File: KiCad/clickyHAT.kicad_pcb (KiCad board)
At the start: 2 copper layers, 65 x 56.5 mm, 22 parts, among them J1 Raspberry_Pi_2_3, Q1 BS170, SW1 SW_Push, SW2 SW_Push, SW3 SW_Push, SW4 SW_Push

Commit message: removed board logo until license is decided
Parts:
- removed REF***: OSHW-Symbol_6.7x6mm_SilkScreen, Symbols:OSHW-Symbol_6.7x6mm_SilkScreen
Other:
- board text added: "Raspberry Pi add-on board for mechanical keyboard switches"
- board text added: "clickyBoard"
- board text removed: "A HAT for mechanical keyboard switches"
- board text removed: "ClickyHAT"

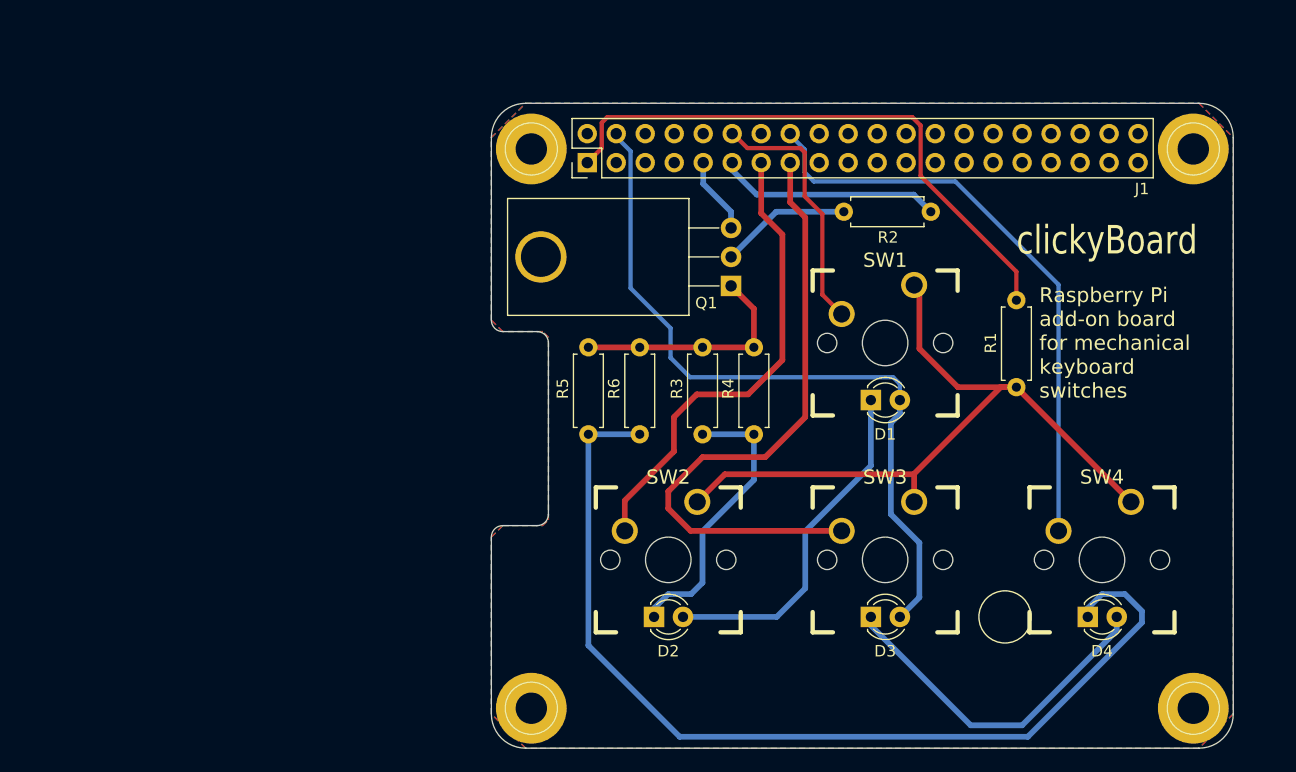
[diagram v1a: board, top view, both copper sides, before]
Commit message: Updated board design
removed copper fill, updated gerbers are included
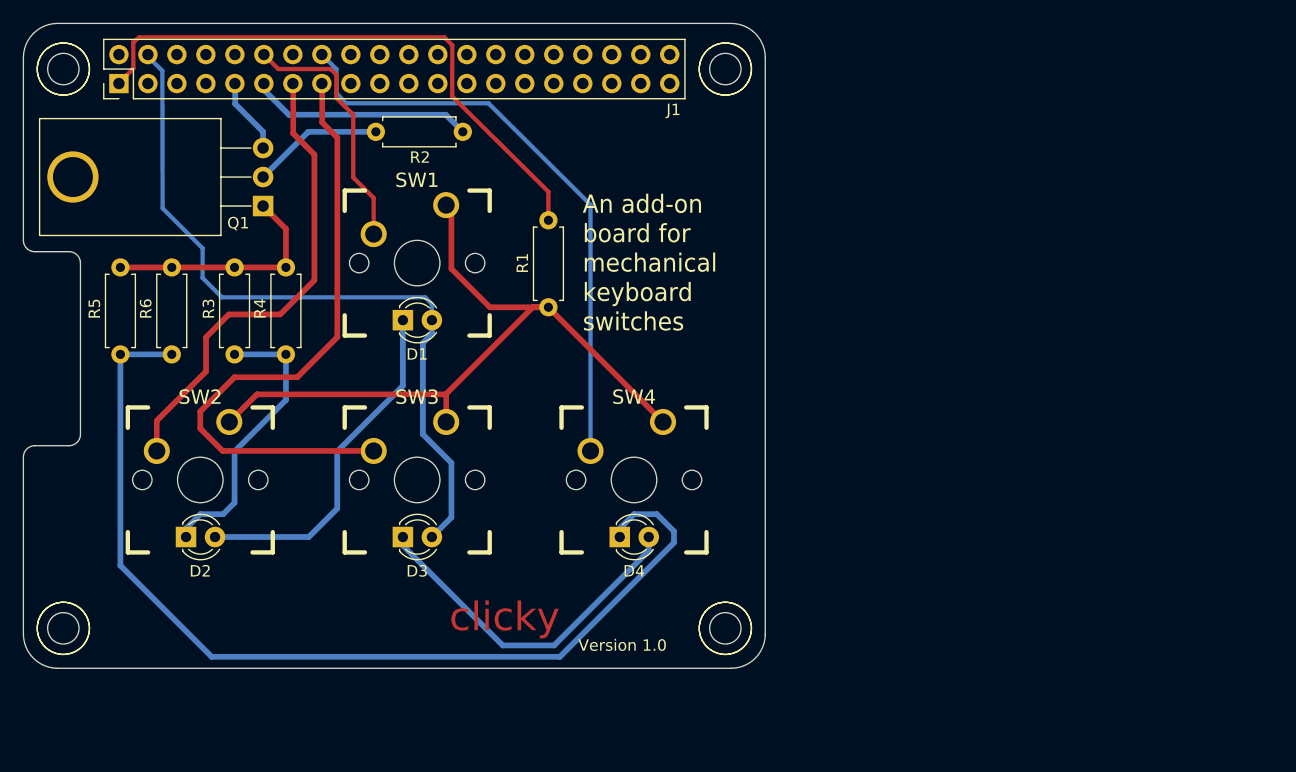
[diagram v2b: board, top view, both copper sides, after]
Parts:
- removed CAM: 1pin, Connectors:1pin
- added MNT1: 1pin, Connectors:1pin, F.Cu at (47.5, 77.0)
- added MNT3: 1pin, Connectors:1pin, F.Cu at (47.5, 126.0)
- added MNT4: 1pin, Connectors:1pin, F.Cu at (105.5, 126.0)
- added MNTB2: 1pin, Connectors:1pin, F.Cu at (105.5, 77.0)
- added REF***: OSHW-Logo_11.4x12mm_SilkScreen, Symbols:OSHW-Logo_11.4x12mm_SilkScreen, B.Cu at (100.0, 95.0)
- moved J1 41.6 mm to (52.4, 78.3)
- moved D1 41.6 mm to (77.2, 99.0)
- moved D2 41.6 mm to (58.2, 118.0)
- moved D3 41.6 mm to (77.2, 118.0)
- moved D4 41.6 mm to (96.2, 118.0)
- moved MNT2 41.6 mm to (105.5, 77.0)
- moved MNTB1 41.6 mm to (47.5, 77.0)
- moved MNTB3 41.6 mm to (47.5, 126.0)
- moved MNTB4 41.6 mm to (105.5, 126.0)
- moved Q1 41.6 mm to (65.0, 89.0)
- moved R1 41.6 mm to (90.0, 90.2)
- moved R2 41.6 mm to (82.5, 82.5)
- moved R3 41.6 mm to (62.5, 102.0)
- moved R4 41.6 mm to (67.0, 102.0)
- moved R5 41.6 mm to (52.5, 102.0)
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- renumbered MNT1 to MNTB1, MNT3 to MNTB3, MNT4 to MNTB4
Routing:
- removed copper zone on B.Cu, net (none)
- removed copper zone on F.Cu, net (none)
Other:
- net class Default: trace_width 0.25 -> 0.375
- board text added: "An add-on board for mechanical keyboard switches"
- board text added: "Board"
- board text added: "CC BY-SA 4.0"
- board text added: "Version 1.0"
- board text added: "clicky"
- board text added: "design by Jack Kelly"
- board text removed: "Raspberry Pi add-on board for mechanical keyboard switches"
- board text removed: "clickyBoard"

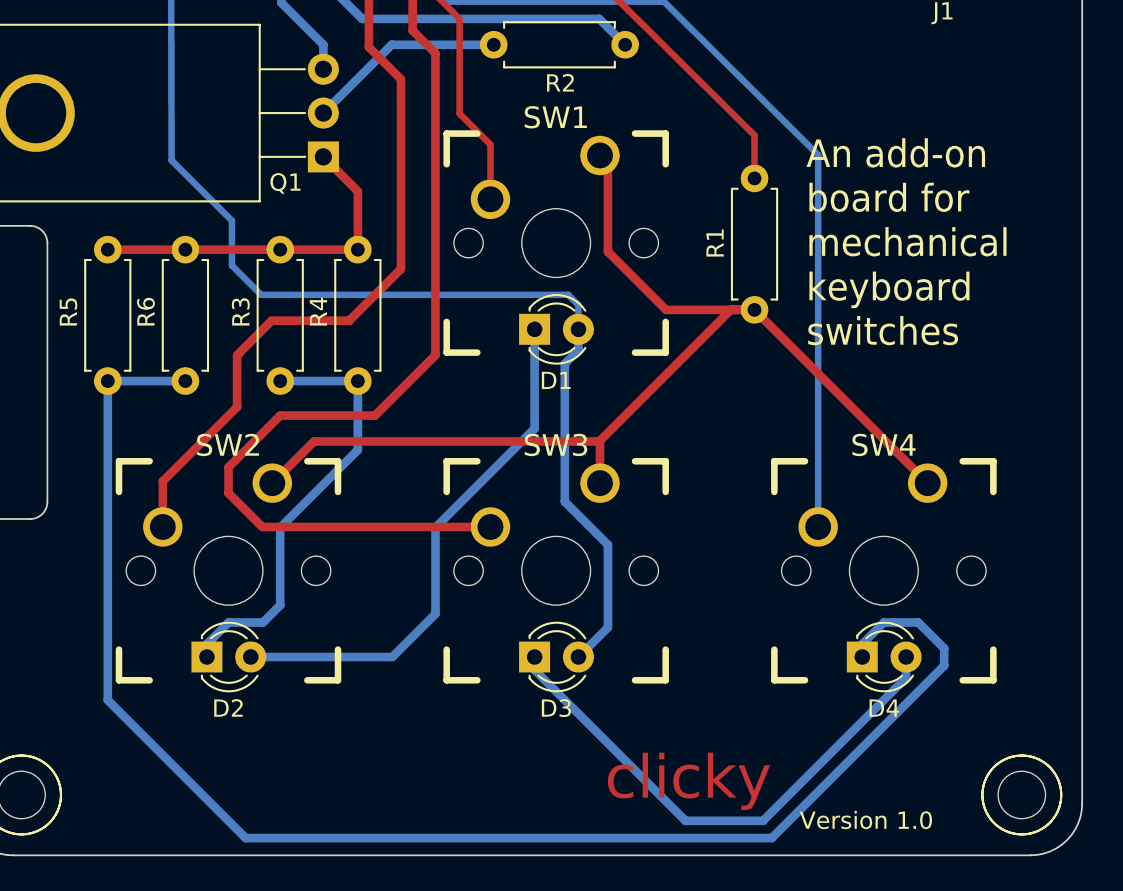
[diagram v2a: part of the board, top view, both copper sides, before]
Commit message: updated board text
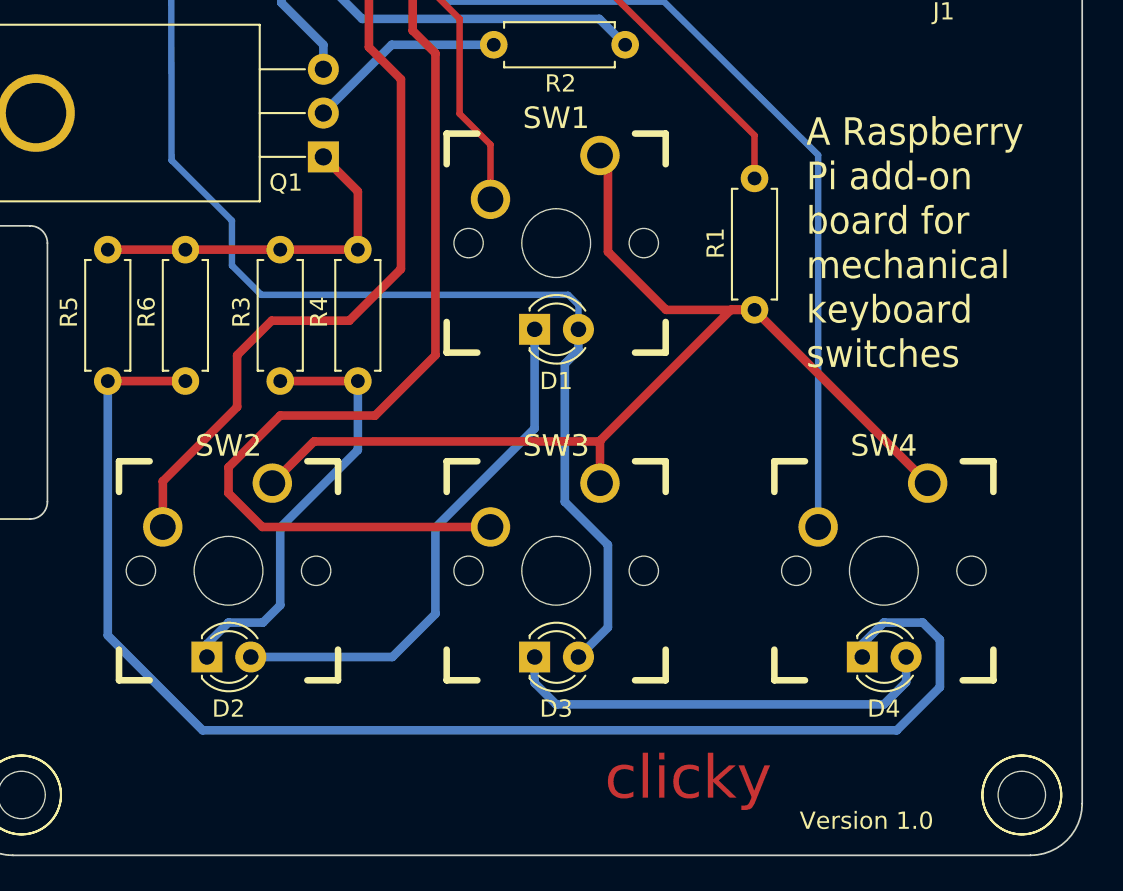
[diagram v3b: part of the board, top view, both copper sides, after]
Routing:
- net Net-(D4-Pad1): track 86.6 -> 79.7 mm
- net Net-(D3-Pad1): track 30.6 -> 26.3 mm
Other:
- board text added: "A Raspberry Pi add-on board for mechanical keyboard switches"
- board text removed: "An add-on board for mechanical keyboard switches"
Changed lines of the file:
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@@
     (thickness 1.6)
     (drawings 24)
-    (tracks 113)
+    (tracks 114)
     (zones 0)
     (modules 25)
@@
   )
   (layers
-    (0 F.Cu signal hide)
+    (0 F.Cu signal)
     (31 B.Cu signal)
     (32 B.Adhes user)
@@
     (arrow2b (pts (xy 47.5 70.5) (xy 48.626504 69.913579)))
   )
-  (gr_text "An add-on\nboard for\nmechanical\nkeyboard\nswitches" (at 93 94) (layer F.SilkS)
+  (gr_text "A Raspberry\nPi add-on\nboard for\nmechanical\nkeyboard\nswitches" (at 93 94) (layer F.SilkS)
     (effects (font (size 1.6 1.5) (thickness 0.15)) (justify left))
   )
@@
   (segment (start 79 101) (end 79 109) (width 0.5) (layer B.Cu) (net 2))
   (segment (start 79.79 100.21) (end 79 101) (width 0.5) (layer B.Cu) (net 2))
-  (segment (start 67 102) (end 62.5 102) (width 0.5) (layer B.Cu) (net 3))
+  (segment (start 67 102) (end 62.5 102) (width 0.5) (layer F.Cu) (net 3))
   (segment (start 58.25 118) (end 58.25 117.25) (width 0.5) (layer B.Cu) (net 3))
   (segment (start 58.25 117.25) (end 59.5 116) (width 0.5) (layer B.Cu) (net 3))
@@
   (segment (start 62.5 110.5) (end 67 106) (width 0.5) (layer B.Cu) (net 3))
   (segment (start 67 106) (end 67 102) (width 0.5) (layer B.Cu) (net 3))
+  (segment (start 77.25 118) (end 77.25 119.5) (width 0.5) (layer B.Cu) (net 4))
+  (segment (start 98.79 119.46) (end 98.79 118) (width 0.5) (layer B.Cu) (net 4))
+  (segment (start 97.5 120.75) (end 98.79 119.46) (width 0.5) (layer B.Cu) (net 4))
+  (segment (start 78.5 120.75) (end 97.5 120.75) (width 0.5) (layer B.Cu) (net 4))
+  (segment (start 77.25 119.5) (end 78.5 120.75) (width 0.5) (layer B.Cu) (net 4))
   (segment (start 77.25 118) (end 77.25 118.75) (width 0.5) (layer B.Cu) (net 4))
-  (segment (start 77.25 118.75) (end 86 127.5) (width 0.5) (layer B.Cu) (net 4))
-  (segment (start 86 127.5) (end 90.5 127.5) (width 0.5) (layer B.Cu) (net 4))
-  (segment (start 90.5 127.5) (end 98.79 119.21) (width 0.5) (layer B.Cu) (net 4))
-  (segment (start 98.79 119.21) (end 98.79 118) (width 0.5) (layer B.Cu) (net 4))
-  (segment (start 52.5 102) (end 57 102) (width 0.5) (layer B.Cu) (net 5))
+  (segment (start 57 102) (end 52.5 102) (width 0.5) (layer F.Cu) (net 5))
   (segment (start 96.25 118) (end 96.25 117.25) (width 0.5) (layer B.Cu) (net 5))
   (segment (start 96.25 117.25) (end 97.5 116) (width 0.5) (layer B.Cu) (net 5))
-  (segment (start 97.5 116) (end 99.5 116) (width 0.5) (layer B.Cu) (net 5))
-  (segment (start 99.5 116) (end 101 117.5) (width 0.5) (layer B.Cu) (net 5))
-  (segment (start 101 117.5) (end 101 118.5) (width 0.5) (layer B.Cu) (net 5))
-  (segment (start 101 118.5) (end 91 128.5) (width 0.5) (layer B.Cu) (net 5))
-  (segment (start 91 128.5) (end 60.5 128.5) (width 0.5) (layer B.Cu) (net 5))
-  (segment (start 60.5 128.5) (end 52.5 120.5) (width 0.5) (layer B.Cu) (net 5))
-  (segment (start 52.5 120.5) (end 52.5 102) (width 0.5) (layer B.Cu) (net 5))
+  (segment (start 97.5 116) (end 99.75 116) (width 0.5) (layer B.Cu) (net 5))
+  (segment (start 99.75 116) (end 100.75 117) (width 0.5) (layer B.Cu) (net 5))
+  (segment (start 100.75 117) (end 100.75 119.75) (width 0.5) (layer B.Cu) (net 5))
+  (segment (start 100.75 119.75) (end 98.25 122.25) (width 0.5) (layer B.Cu) (net 5))
+  (segment (start 98.25 122.25) (end 58 122.25) (width 0.5) (layer B.Cu) (net 5))
+  (segment (start 58 122.25) (end 52.5 116.75) (width 0.5) (layer B.Cu) (net 5))
+  (segment (start 52.5 116.75) (end 52.5 102) (width 0.5) (layer B.Cu) (net 5))
   (segment (start 90 90.25) (end 90 87.75) (width 0.375) (layer F.Cu) (net 6))
   (segment (start 53.637747 76.93845) (end 52.4 78.2) (width 0.375) (layer F.Cu) (net 6))

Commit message: Revision 1.1
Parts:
- R3, R4, R5, R6: value 100 -> 150
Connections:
- D2 pad 2: Net-(D1-Pad1) -> Net-(D1-Pad2)
- D4 pad 2: Net-(D3-Pad1) -> Net-(D1-Pad2)
- J1 pad 39: Net-(J1-Pad39) -> Net-(J1-Pad25)
- J1 pad 9: Net-(J1-Pad9) -> Net-(J1-Pad25)
- Q1 pad 1: Net-(Q1-Pad1) -> Net-(Q1-Pad2)
- Q1 pad 2: Net-(Q1-Pad2) -> Net-(Q1-Pad1)
- Q1 pad 3: Net-(J1-Pad9) -> Net-(J1-Pad25)
- R4 pad 1: Net-(D2-Pad1) -> Net-(D1-Pad1)
- R6 pad 1: Net-(D4-Pad1) -> Net-(D3-Pad1)
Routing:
- net Net-(D1-Pad2): track 65.1 -> 134.0 mm
- net Net-(J1-Pad15): track 55.0 -> 34.8 mm
- net Net-(D1-Pad1): track 30.6 -> 11.5 mm
- net Net-(D3-Pad1): track 26.3 -> 43.6 mm
- net Net-(D4-Pad1): track 79.7 -> 63.6 mm
- net Net-(J1-Pad9): track 6.73 -> 0.00 mm
- net Net-(J1-Pad25): track 0.00 -> 6.72 mm
- net Net-(J1-Pad12): track 22.4 -> 27.8 mm
- net Net-(J1-Pad16): track 52.7 -> 49.2 mm
- net Net-(Q1-Pad1): track 20.7 -> 23.8 mm
- net Net-(R1-Pad2): track 64.4 -> 61.7 mm
- net Net-(J1-Pad1): track 51.3 -> 48.7 mm
- net Net-(J1-Pad13): track 41.7 -> 40.6 mm
- net Net-(Q1-Pad2): track 11.5 -> 12.7 mm
- net Net-(D2-Pad1): track 25.3 -> 24.7 mm
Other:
- board text added: "Version 1.1"
- board text removed: "Version 1.0"

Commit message: Documentation updated
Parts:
- moved R3 10.0 mm to (52.5, 102.0)
- moved R4 10.0 mm to (57.0, 102.0)
- moved R5 10.0 mm to (62.5, 102.0)
- moved R6 10.0 mm to (67.0, 102.0)
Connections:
- J1 pad 39: Net-(J1-Pad25) -> Net-(J1-Pad39)
- J1 pad 9: Net-(J1-Pad25) -> Net-(J1-Pad9)
- Q1 pad 3: Net-(J1-Pad25) -> Net-(J1-Pad9)
- R3 pad 1: Net-(D2-Pad1) -> Net-(D4-Pad1)
- R4 pad 1: Net-(D1-Pad1) -> Net-(D3-Pad1)
- R5 pad 1: Net-(D4-Pad1) -> Net-(D2-Pad1)
- R6 pad 1: Net-(D3-Pad1) -> Net-(D1-Pad1)
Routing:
- net Net-(J1-Pad9): track 0.00 -> 6.72 mm
- net Net-(J1-Pad25): track 6.72 -> 0.00 mm
- added copper zone on F.Cu, net Net-(Q1-Pad1)
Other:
- board text added: "GPIO 12"
- board text added: "GPIO 13"
- board text added: "GPIO 15"
- board text added: "GPIO 16"
- board text added: "LEDs GPIO 11"

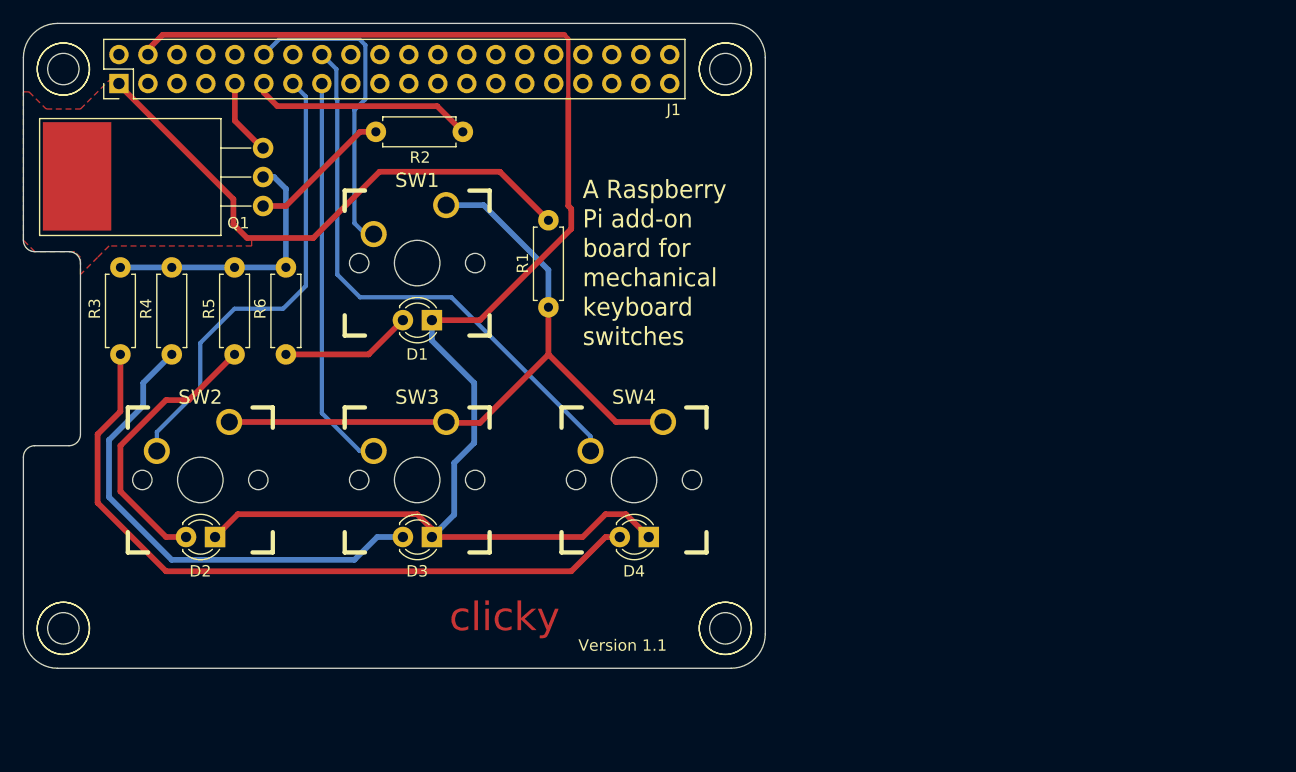
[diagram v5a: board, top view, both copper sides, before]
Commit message: Rotated switches
crazy routing
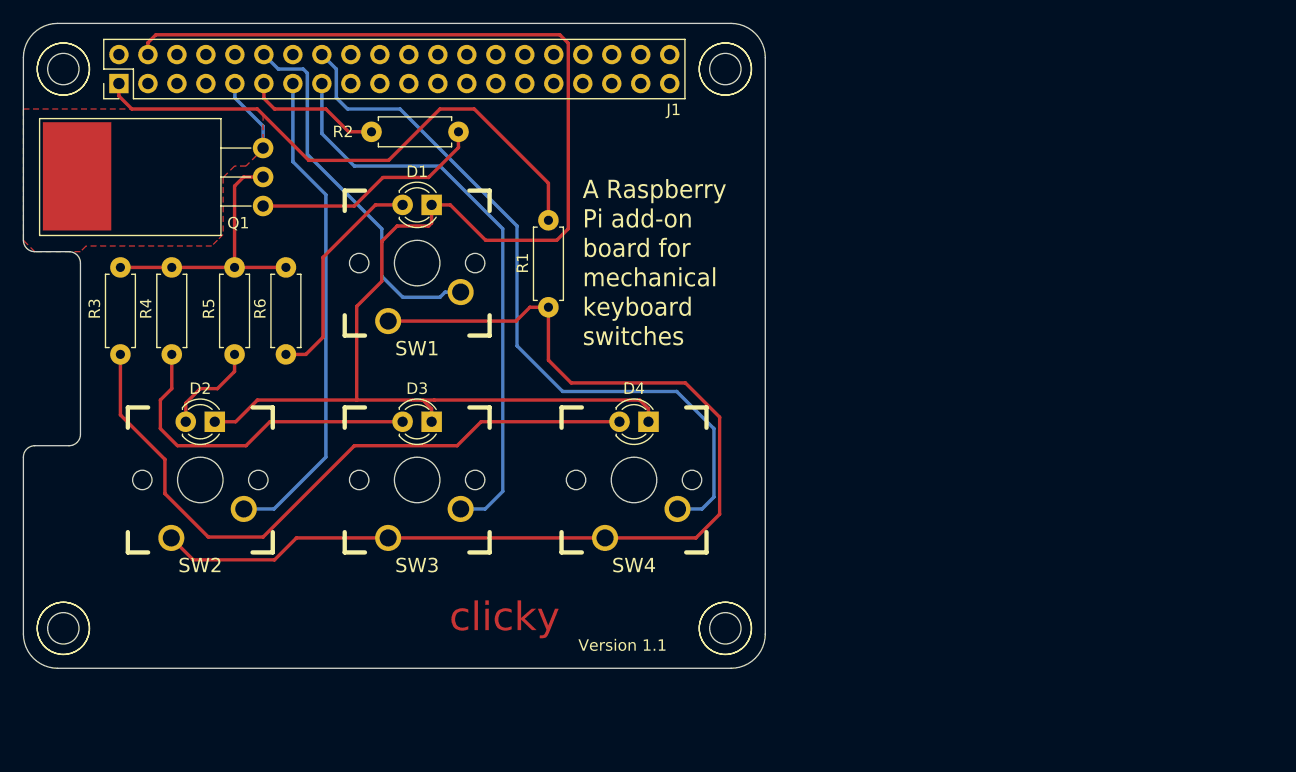
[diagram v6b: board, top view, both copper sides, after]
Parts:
- moved D1 10.1 mm to (77.2, 88.9)
- moved D2 10.1 mm to (58.2, 107.9)
- moved D3 10.1 mm to (77.2, 107.9)
- moved D4 10.1 mm to (96.2, 107.9)
- moved R2 8.00 mm to (74.5, 82.5), turned to 0 degrees
- turned SW1 to 180 degrees
- turned SW2 to 180 degrees
- turned SW3 to 180 degrees
- turned SW4 to 180 degrees
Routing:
- net Net-(R1-Pad2): track 61.7 -> 95.2 mm
- net Net-(J1-Pad15): track 34.8 -> 51.0 mm
- net Net-(D2-Pad1): track 24.7 -> 8.55 mm
- net Net-(J1-Pad16): track 49.2 -> 65.2 mm
- net Net-(D3-Pad1): track 43.6 -> 29.6 mm
- net Net-(D1-Pad1): track 11.5 -> 19.8 mm
- net Net-(Q1-Pad2): track 12.7 -> 20.6 mm
- net Net-(J1-Pad11): track 19.7 -> 11.9 mm
- net Net-(J1-Pad12): track 27.8 -> 32.8 mm
- net Net-(D4-Pad1): track 63.6 -> 59.4 mm
- net Net-(J1-Pad13): track 40.6 -> 43.0 mm
- net Net-(D1-Pad2): track 134.0 -> 132.3 mm
- net Net-(Q1-Pad1): track 23.8 -> 24.5 mm
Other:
- net class Default: clearance 0.2 -> 0.25; trace_width 0.375 -> 0.3
- rule trace_clearance: 0.2 -> 0.25
